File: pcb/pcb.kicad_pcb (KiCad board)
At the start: 2 copper layers, 109 x 54 mm, 63 parts, among them J1 MALE, J10 TC2030_NL, J101 MALE, J102 FEMALE, J103 MALE, J104 FEMALE, J105 MALE, J106 FEMALE, J107 MALE, J108 FEMALE, J11 STANDOFF, J111 STANDOFF, J112 STANDOFF, J113 STANDOFF, J114 STANDOFF, J12 STANDOFF, J13 STANDOFF, J14 STANDOFF, J2 FEMALE, J3 MALE, J4 FEMALE, J5 MALE, J6 FEMALE, J7 MALE, J8 FEMALE, J9 DTR, Q1 2N3904, SW1 ACTION, SW2 ACTION, SW3 ACTION, SW4 ACTION, U3 ATmega328P-MU, Y1 YSX321SL

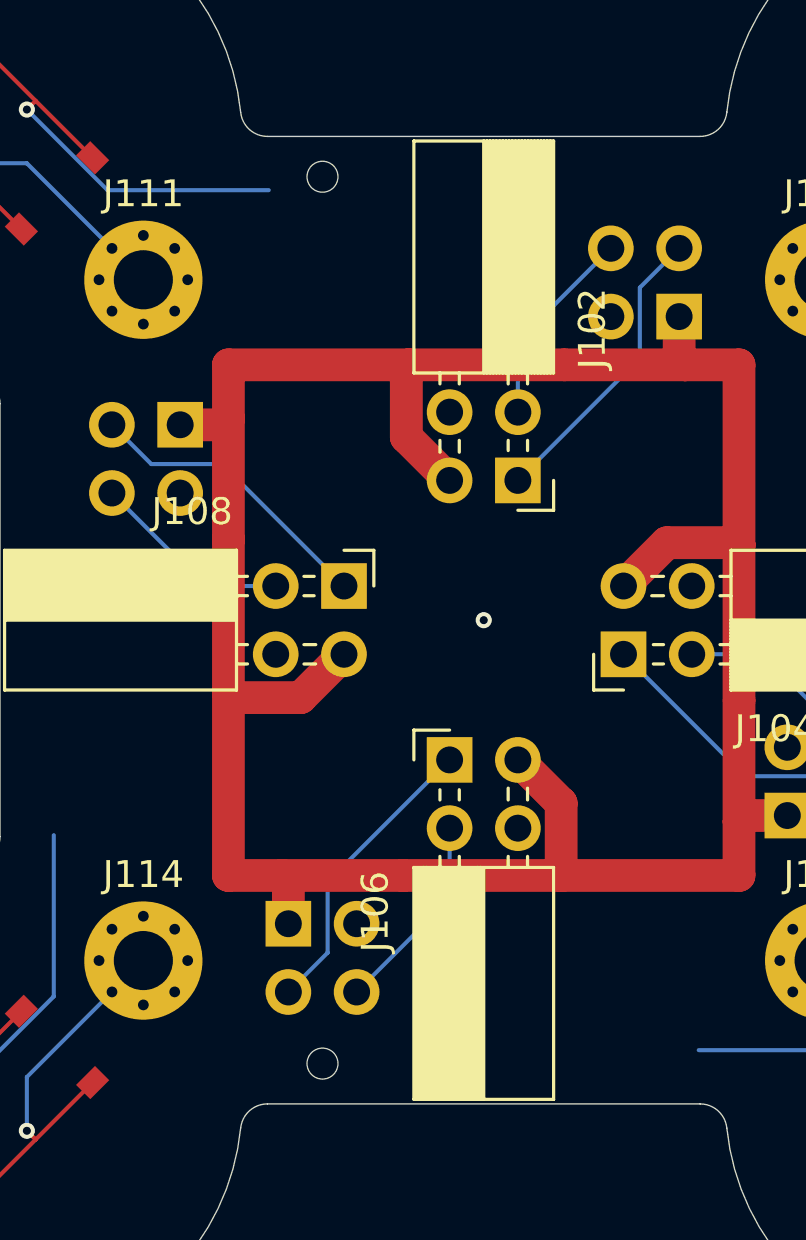
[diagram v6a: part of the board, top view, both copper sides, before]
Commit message: Hide tooling holes under female headers
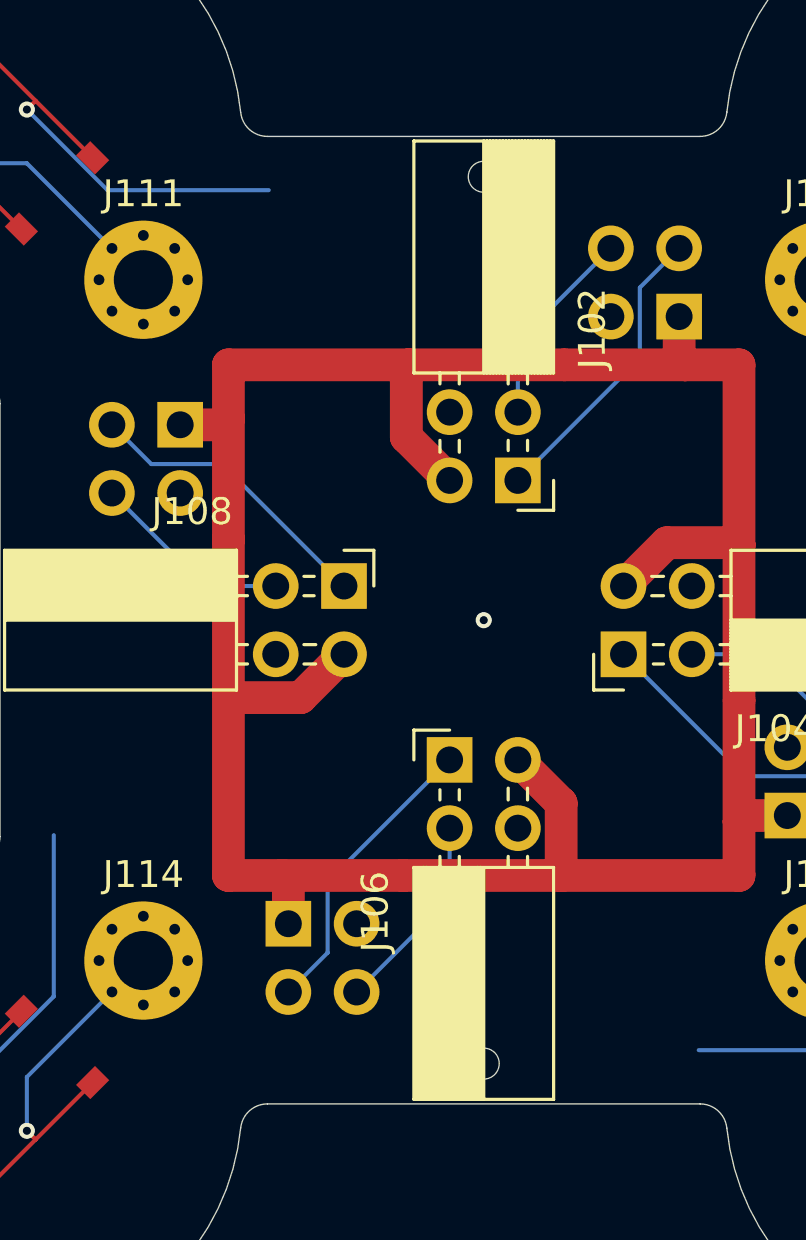
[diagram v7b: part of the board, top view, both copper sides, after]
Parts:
- moved jlcpcb-tooling-hole 6.00 mm to (121.0, 88.5)
- moved jlcpcb-tooling-hole 6.00 mm to (121.0, 121.5)
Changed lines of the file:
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@@
     (45 Margin user hide)
     (46 B.CrtYd user hide)
-    (47 F.CrtYd user hide)
+    (47 F.CrtYd user)
     (48 B.Fab user hide)
     (49 F.Fab user hide)
@@
   )
   (module node:JLCPCB-tooling-hole (layer F.Cu)
-    (at 115 88.5)
+    (at 121 88.5)
     (descr https://support.jlcpcb.com/article/92-how-to-add-tooling-holes-for-smt-assembly-order)
     (attr smd)
@@
   )
   (module node:JLCPCB-tooling-hole (layer F.Cu)
-    (at 115 121.5)
+    (at 121 121.5)
     (descr https://support.jlcpcb.com/article/92-how-to-add-tooling-holes-for-smt-assembly-order)
     (attr smd)

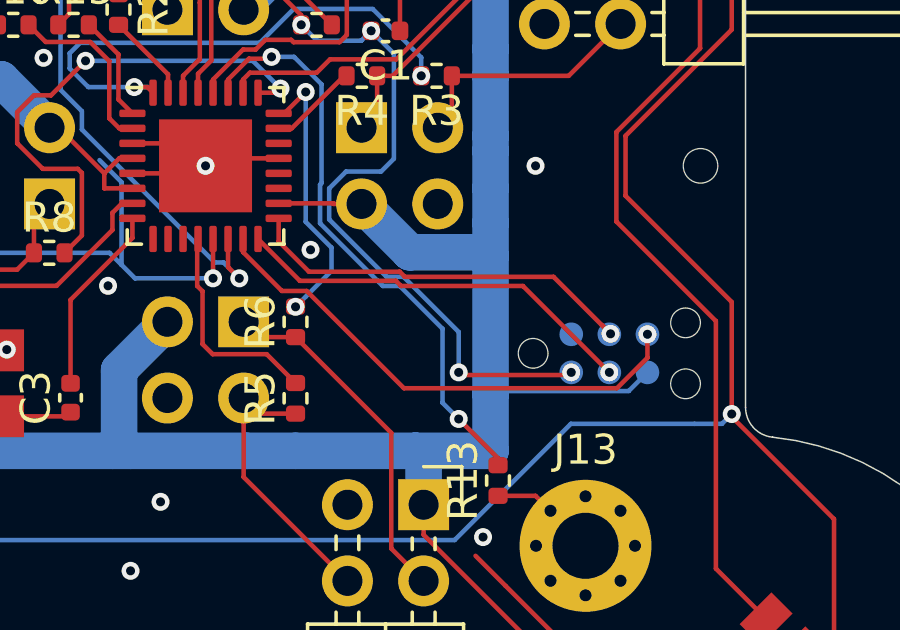
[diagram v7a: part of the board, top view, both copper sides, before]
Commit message: Flip FTDI connector inward for protection
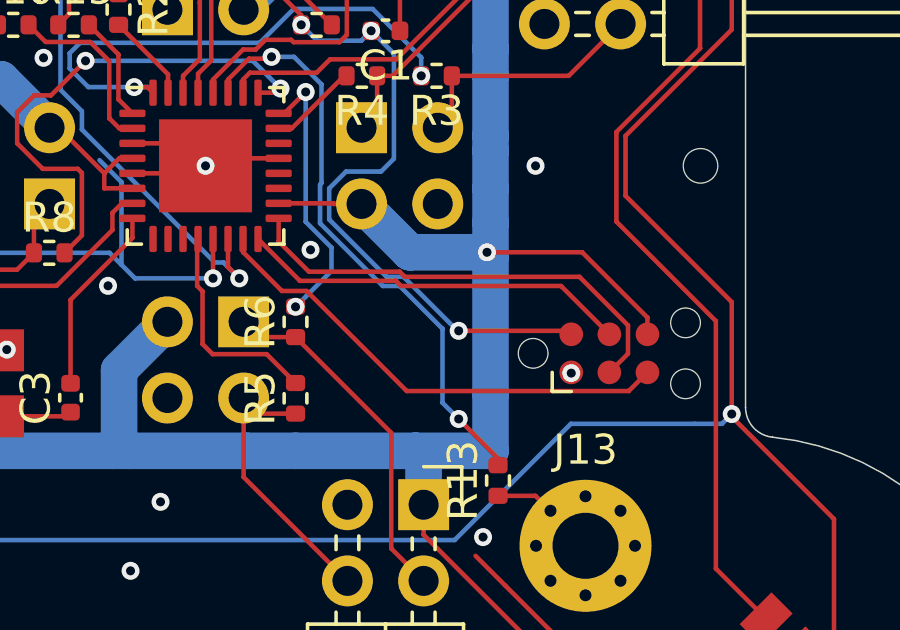
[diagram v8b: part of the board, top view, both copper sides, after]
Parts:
- J10: moved to F.Cu
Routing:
- net /Lower Board/SCK: track 13.6 -> 15.4 mm, vias 1 -> 0
- net +5VB: track 177.7 -> 179.1 mm, vias 3 -> 4
- net /Lower Board/~RST: track 29.6 -> 28.2 mm, vias 4 -> 3
- net /Lower Board/MOSI: track 17.3 -> 16.4 mm, vias 1 -> 0
- net /Lower Board/MISO: track 13.6 -> 13.0 mm, vias 1 -> 0
- net GNDB: track 51.6 -> 51.7 mm, vias 20 -> 21
